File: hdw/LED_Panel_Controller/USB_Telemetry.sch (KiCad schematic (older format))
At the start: 7 parts

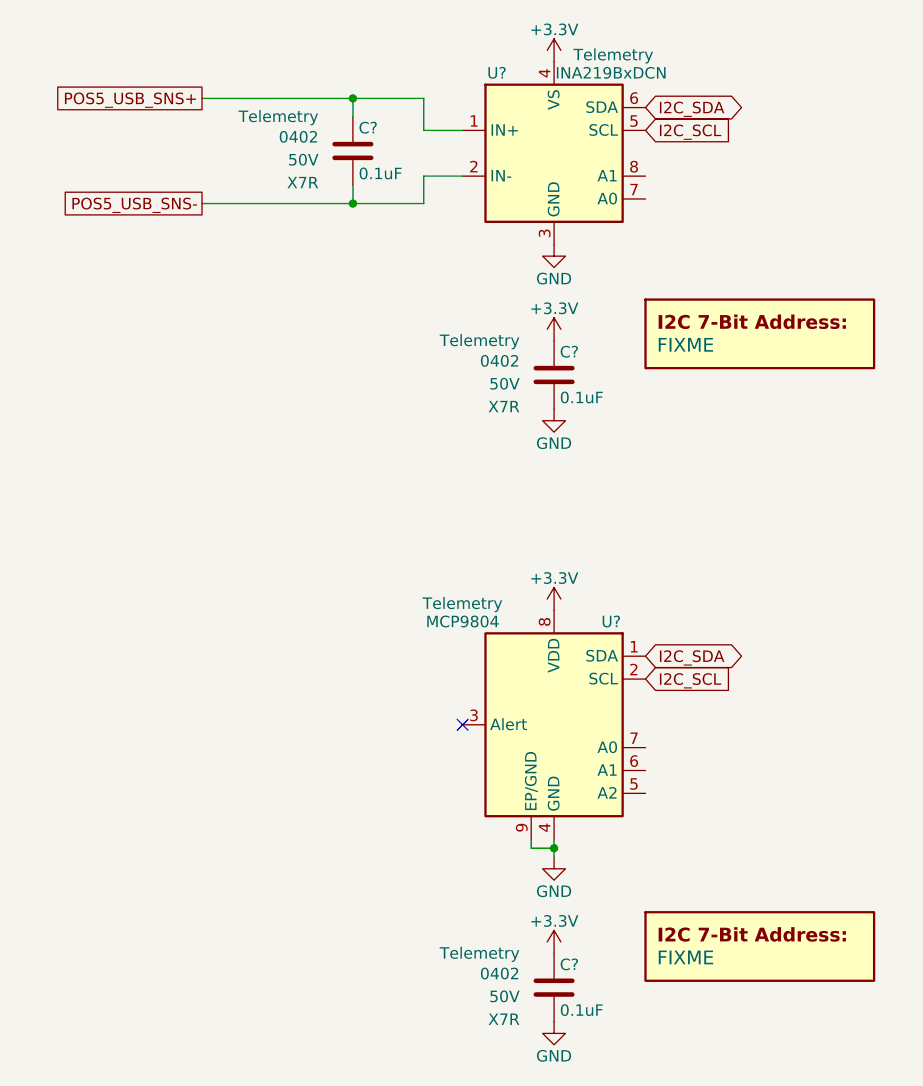
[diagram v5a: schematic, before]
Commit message: assigned I2C addresses
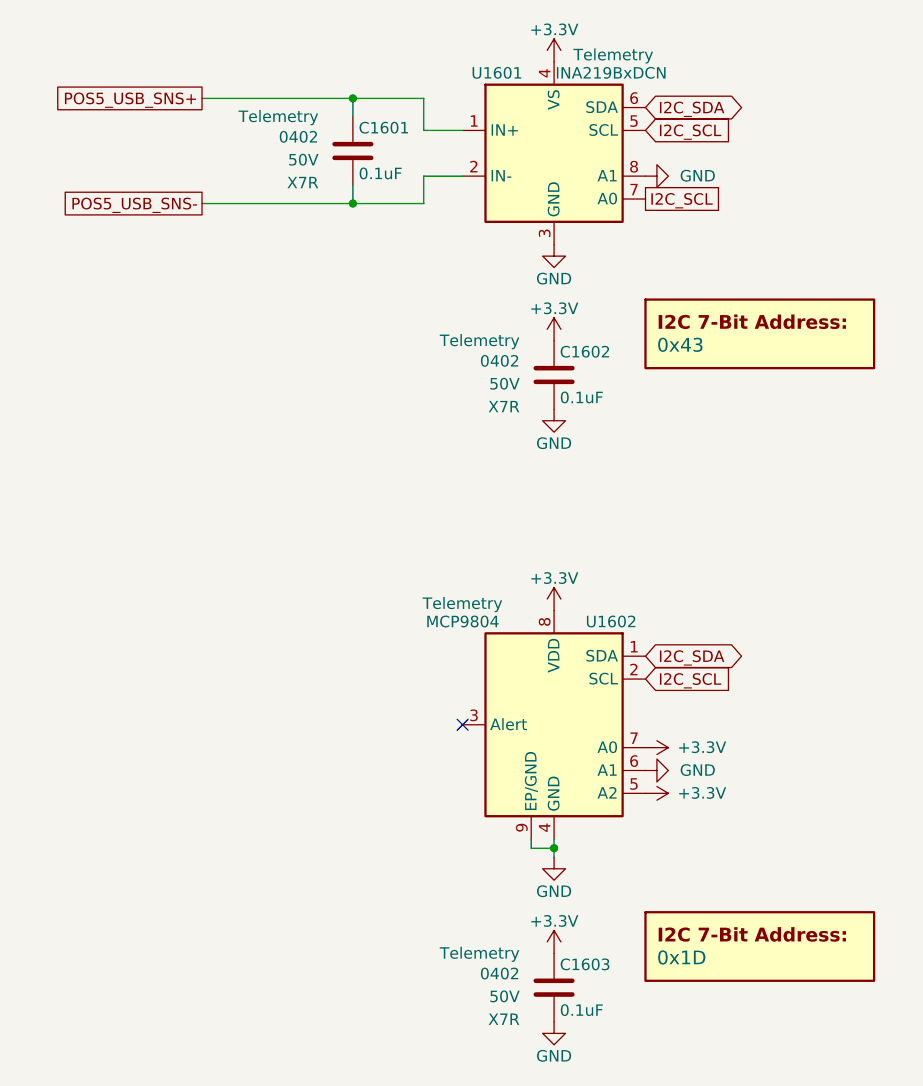
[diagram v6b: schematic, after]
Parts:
- removed C? (x3): 0.1uF, Capacitors_SMD:C_0402, symbol Custom_Library:C_Custom
- removed DOC? (x2): FIXME, symbol Custom_Library:I2C_Address
- removed U?: INA219BxDCN, Package_TO_SOT_SMD:SOT-23-8, symbol Analog_ADC:INA219BxDCN
- added C1601, C1602, C1603: 0.1uF, Capacitors_SMD:C_0402, symbol Custom_Library:C_Custom
- added DOC1601: 0x43, symbol Custom_Library:I2C_Address
- added DOC1602: 0x1D, symbol Custom_Library:I2C_Address
- added U1601: INA219BxDCN, Package_TO_SOT_SMD:SOT-23-8, symbol Analog_ADC:INA219BxDCN
- gave numbers to parts that had none: 1
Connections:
- net +3V3: now also U1602.5 (A2), U1602.7 (A0), C1602.1, C1603.1, U1601.4 (VS)
- net GND: now also U1602.6 (A1), C1602.2, C1603.2, U1601.3 (GND), U1601.8 (A1)
- net I2C_SCL: now also U1601.5 (SCL), U1601.7 (A0)
- net I2C_SDA: now also U1601.6 (SDA)
- net POS5_USB_SNS+: now also C1601.1, U1601.1 (IN+)
- net POS5_USB_SNS-: now also C1601.2, U1601.2 (IN-)
